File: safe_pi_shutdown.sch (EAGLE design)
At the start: 35 parts, among them IC1 MCP73831, IC2 LTC2952CF, IC3 MIC2876, Q1 IRF7342, Q2 IRF7342, X1 MICRO-USB-RECEPTACLE47589-0001, X4 MF-CON-2.54mm-01x02, X5 MF-CON-2.54mm-01x02

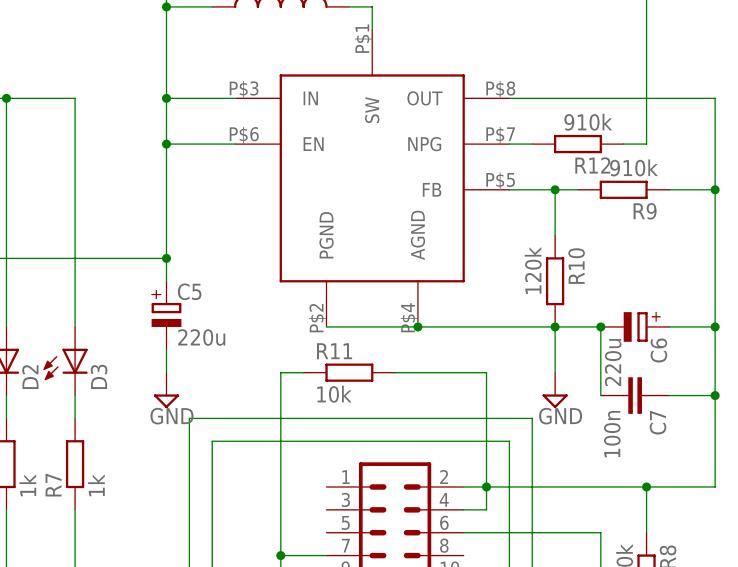
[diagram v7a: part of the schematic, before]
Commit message: add more capacitors to power path
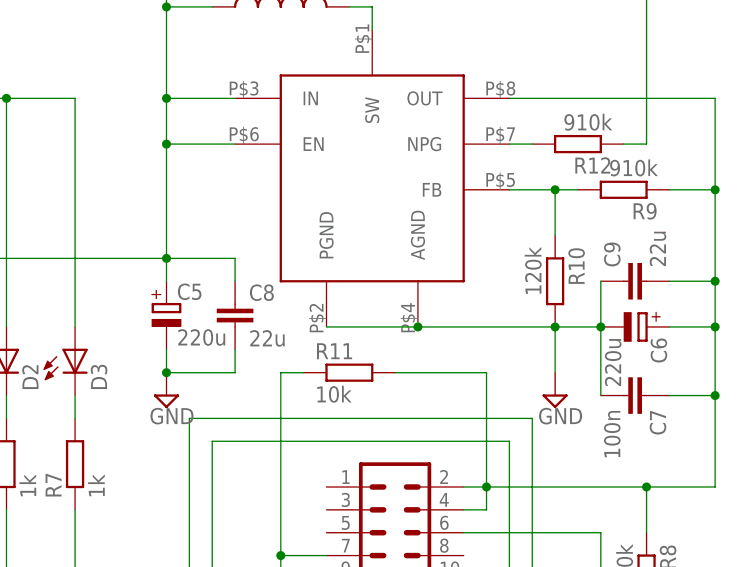
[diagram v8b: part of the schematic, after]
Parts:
- added C8, C9: 22u, rcl:C-EUC0603
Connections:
- net GND: now also C8.2, C9.1
- net N$4: now also C9.2
- net VCC: now also C8.1
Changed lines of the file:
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@@
 <?xml version="1.0" encoding="utf-8"?>
 <!DOCTYPE eagle SYSTEM "eagle.dtd">
-<eagle version="6.5.0">
+<eagle version="6.6.0">
 <drawing>
 <settings>
@@
 <part name="C6" library="rcl" deviceset="CPOL-EU" device="E3.5-8" value="220u"/>
 <part name="C7" library="rcl" deviceset="C-EU" device="C0402" value="100n"/>
+<part name="C8" library="rcl" deviceset="C-EU" device="C0603" value="22u"/>
+<part name="C9" library="rcl" deviceset="C-EU" device="C0603" value="22u"/>
 </parts>
 <sheets>
@@
 <instance part="C6" gate="G$1" x="215.9" y="142.24" rot="R270"/>
 <instance part="C7" gate="G$1" x="215.9" y="134.62" rot="R270"/>
+<instance part="C8" gate="G$1" x="170.18" y="144.78"/>
+<instance part="C9" gate="G$1" x="213.36" y="147.32" rot="R90"/>
 </instances>
 <busses>
@@
 <wire x1="210.82" y1="134.62" x2="210.82" y2="142.24" width="0.1524" layer="91"/>
 <junction x="210.82" y="142.24"/>
+<pinref part="C9" gate="G$1" pin="1"/>
+<wire x1="210.82" y1="147.32" x2="210.82" y2="142.24" width="0.1524" layer="91"/>
 </segment>
 <segment>
@@
 <wire x1="162.56" y1="139.7" x2="162.56" y2="137.16" width="0.1524" layer="91"/>
 <pinref part="C5" gate="G$1" pin="-"/>
+<pinref part="C8" gate="G$1" pin="2"/>
+<wire x1="170.18" y1="139.7" x2="170.18" y2="137.16" width="0.1524" layer="91"/>
+<wire x1="170.18" y1="137.16" x2="162.56" y2="137.16" width="0.1524" layer="91"/>
+<junction x="162.56" y="137.16"/>
 </segment>
 </net>
@@
 <pinref part="L1" gate="G$1" pin="1"/>
 <pinref part="C5" gate="G$1" pin="+"/>
+<pinref part="C8" gate="G$1" pin="1"/>
+<wire x1="170.18" y1="147.32" x2="170.18" y2="149.86" width="0.1524" layer="91"/>
+<wire x1="170.18" y1="149.86" x2="162.56" y2="149.86" width="0.1524" layer="91"/>
 </segment>
 </net>
@@
 <wire x1="223.52" y1="157.48" x2="218.44" y2="157.48" width="0.1524" layer="91"/>
 <wire x1="223.52" y1="167.64" x2="223.52" y2="157.48" width="0.1524" layer="91"/>
-<wire x1="223.52" y1="157.48" x2="223.52" y2="142.24" width="0.1524" layer="91"/>
+<wire x1="223.52" y1="157.48" x2="223.52" y2="147.32" width="0.1524" layer="91"/>
+<wire x1="223.52" y1="147.32" x2="223.52" y2="142.24" width="0.1524" layer="91"/>
 <wire x1="223.52" y1="142.24" x2="223.52" y2="134.62" width="0.1524" layer="91"/>
 <wire x1="223.52" y1="134.62" x2="223.52" y2="124.46" width="0.1524" layer="91"/>
@@
 <wire x1="218.44" y1="142.24" x2="223.52" y2="142.24" width="0.1524" layer="91"/>
 <junction x="223.52" y="142.24"/>
-</segment>
-</net>
+<pinref part="C9" gate="G$1" pin="2"/>
+<wire x1="218.44" y1="147.32" x2="223.52" y2="147.32" width="0.1524" layer="91"/>
+<junction x="223.52" y="147.32"/>
+</segment>
+</net>
